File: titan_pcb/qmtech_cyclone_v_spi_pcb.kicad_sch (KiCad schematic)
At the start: 47 parts, among them J1 FPGA, J10 OLED_CONN, J11 OLED_CONN, J12 CH341_PRG_CONN, J13 SPI_HEADER, J14 SPI_HEADER, J15 I2C_PULLUP, J16 I2C_PULLUP, J17 I2C_PULLUP, J18 I2C_PULLUP, J19 Barrel_Jack_MountingPin, J2 FPGA, J20 PWR_SW, J21 PWR_SW, J22 PWR_SW, J23 PWR_SW, J3 TEENSY, J4 TEENSY, J5 ESP, J6 ESP, J7 PICO, J8 PICO, J9 OLED_JMP, U1 LM1084-3.3

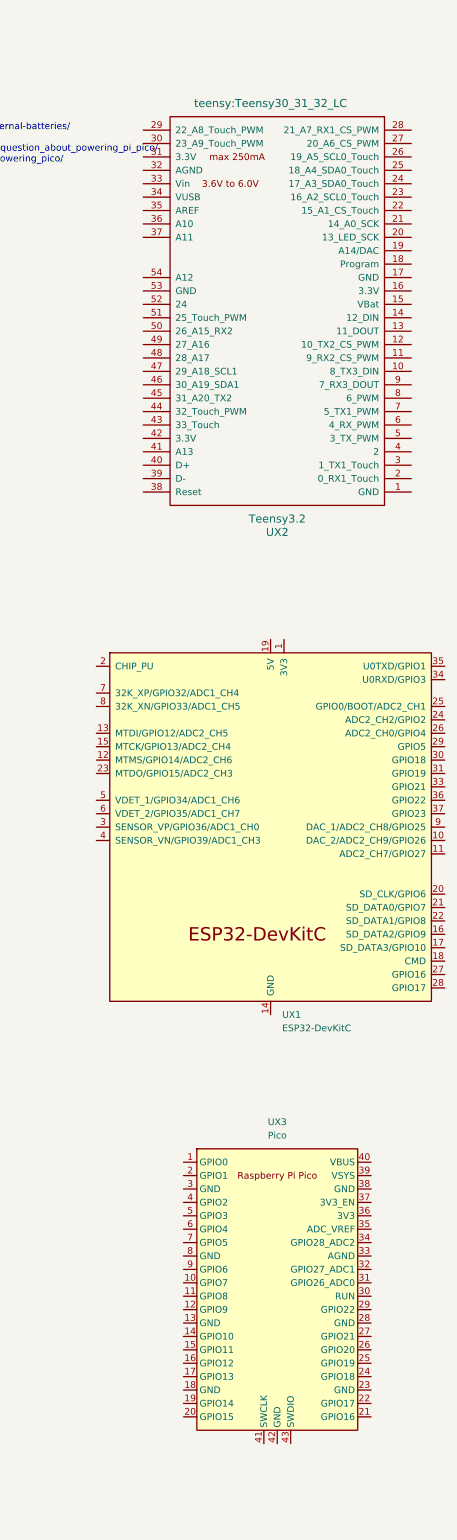
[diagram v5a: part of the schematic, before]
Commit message: removed mcus, updated silkscreen, regenerated bom
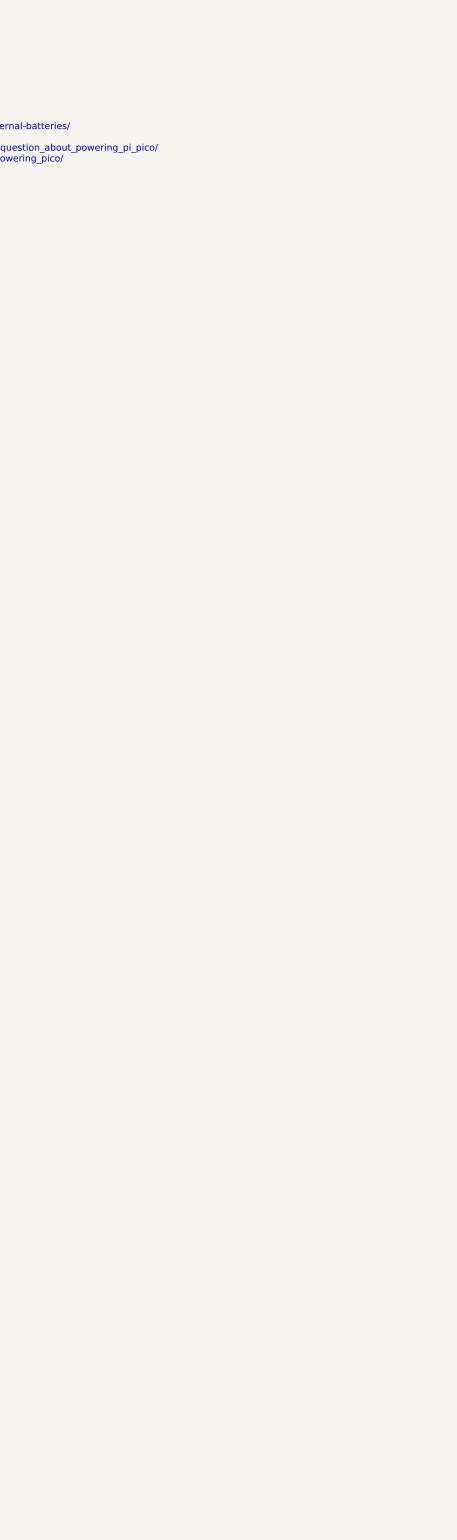
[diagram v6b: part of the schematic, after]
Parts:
- removed UX1: ESP32-DevKitC, PCM_Espressif:ESP32-DevKitC, symbol PCM_Espressif:ESP32-DevKitC
- removed UX2: Teensy3.2, teensy:Teensy30_31_32_LC, symbol teensy:Teensy3.2
- removed UX3: Pico, MCU_RaspberryPi_and_Boards:RPi_Pico_SMD_TH, symbol MCU_RaspberryPi_and_Boards:Pico
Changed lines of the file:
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@@
     )
   )
-  (symbol (lib_id "PCM_Espressif:ESP32-DevKitC") (at 491.49 163.83 0) (unit 1)
-    (in_bom no) (on_board no) (dnp no) (fields_autoplaced)
-    (property "Reference" "UX1" (at 493.6841 199.39 0)
-      (effects (font (size 1.27 1.27)) (justify left))
-    )
-    (property "Value" "ESP32-DevKitC" (at 493.6841 201.93 0)
-      (effects (font (size 1.27 1.27)) (justify left))
-    )
-    (property "Footprint" "PCM_Espressif:ESP32-DevKitC" (at 491.49 207.01 0)
-      (effects (font (size 1.27 1.27)) hide)
-    )
-    (property "Datasheet" "https://docs.espressif.com/projects/esp-idf/zh_CN/latest/esp32/hw-reference/esp32/get-started-devkitc.html" (at 491.49 209.55 0)
-      (effects (font (size 1.27 1.27)) hide)
-    )
-    (pin "14")
-    (pin "19")
+  (symbol (lib_id "Connector:AVR-JTAG-10") (at 184.785 318.135 0) (unit 1)
+    (in_bom no) (on_board yes) (dnp no) (fields_autoplaced)
+    (property "Reference" "JX1" (at 172.72 316.865 0)
+      (effects (font (size 1.27 1.27)) (justify right))
+    )
+    (property "Value" "DUMMY_JTAG" (at 172.72 319.405 0)
+      (effects (font (size 1.27 1.27)) (justify right))
+    )
+    (property "Footprint" "Connector_IDC:IDC-Header_2x05_P2.54mm_Vertical" (at 180.975 314.325 90)
+      (effects (font (size 1.27 1.27)) hide)
+    )
+    (property "Datasheet" " ~" (at 152.4 332.105 0)
+      (effects (font (size 1.27 1.27)) hide)
+    )
     (pin "1")
     (pin "10")
-    (pin "11")
-    (pin "12")
-    (pin "13")
-    (pin "15")
-    (pin "16")
-    (pin "17")
-    (pin "18")
-    (pin "2")
-    (pin "20")
-    (pin "21")
-    (pin "22")
-    (pin "23")
-    (pin "24")
-    (pin "25")
-    (pin "26")
-    (pin "27")
-    (pin "28")
-    (pin "29")
-    (pin "3")
-    (pin "30")
-    (pin "31")
-    (pin "32")
-    (pin "33")
-    (pin "34")
-    (pin "35")
-    (pin "36")
-    (pin "37")
-    (pin "38")
+    (pin "2")
+    (pin "3")
     (pin "4")
     (pin "5")
@@
       (project "qmtech_cyclone_v_spi_pcb"
         (path "/6b222715-3ff4-46c6-84bf-6d2ef29db0c3"
-          (reference "UX1") (unit 1)
-        )
-      )
-    )
-  )
-  (symbol (lib_id "Connector:AVR-JTAG-10") (at 184.785 318.135 0) (unit 1)
-    (in_bom no) (on_board yes) (dnp no) (fields_autoplaced)
-    (property "Reference" "JX1" (at 172.72 316.865 0)
-      (effects (font (size 1.27 1.27)) (justify right))
-    )
-    (property "Value" "DUMMY_JTAG" (at 172.72 319.405 0)
-      (effects (font (size 1.27 1.27)) (justify right))
-    )
-    (property "Footprint" "Connector_IDC:IDC-Header_2x05_P2.54mm_Vertical" (at 180.975 314.325 90)
-      (effects (font (size 1.27 1.27)) hide)
-    )
-    (property "Datasheet" " ~" (at 152.4 332.105 0)
-      (effects (font (size 1.27 1.27)) hide)
-    )
-    (pin "1")
-    (pin "10")
-    (pin "2")
-    (pin "3")
-    (pin "4")
-    (pin "5")
-    (pin "6")
-    (pin "7")
-    (pin "8")
-    (pin "9")
-    (instances
-      (project "qmtech_cyclone_v_spi_pcb"
-        (path "/6b222715-3ff4-46c6-84bf-6d2ef29db0c3"
           (reference "JX1") (unit 1)
         )
@@
         (path "/6b222715-3ff4-46c6-84bf-6d2ef29db0c3"
           (reference "J20") (unit 1)
-        )
-      )
-    )
-  )
-  (symbol (lib_id "MCU_RaspberryPi_and_Boards:Pico") (at 492.76 251.46 0) (unit 1)
-    (in_bom no) (on_board no) (dnp no) (fields_autoplaced)
-    (property "Reference" "UX3" (at 492.76 219.71 0)
-      (effects (font (size 1.27 1.27)))
-    )
-    (property "Value" "Pico" (at 492.76 222.25 0)
-      (effects (font (size 1.27 1.27)))
-    )
-    (property "Footprint" "MCU_RaspberryPi_and_Boards:RPi_Pico_SMD_TH" (at 492.76 251.46 90)
-      (effects (font (size 1.27 1.27)) hide)
-    )
-    (property "Datasheet" "" (at 492.76 251.46 0)
-      (effects (font (size 1.27 1.27)) hide)
-    )
-    (pin "1")
-    (pin "10")
-    (pin "11")
-    (pin "12")
-    (pin "13")
-    (pin "14")
-    (pin "15")
-    (pin "16")
-    (pin "17")
-    (pin "18")
-    (pin "19")
-    (pin "2")
-    (pin "20")
-    (pin "21")
-    (pin "22")
-    (pin "23")
-    (pin "24")
-    (pin "25")
-    (pin "26")
-    (pin "27")
-    (pin "28")
-    (pin "29")
-    (pin "3")
-    (pin "30")
-    (pin "31")
-    (pin "32")
-    (pin "33")
-    (pin "34")
-    (pin "35")
-    (pin "36")
-    (pin "37")
-    (pin "38")
-    (pin "39")
-    (pin "4")
-    (pin "40")
-    (pin "41")
-    (pin "42")
-    (pin "43")
-    (pin "5")
-    (pin "6")
-    (pin "7")
-    (pin "8")
-    (pin "9")
-    (instances
-      (project "qmtech_cyclone_v_spi_pcb"
-        (path "/6b222715-3ff4-46c6-84bf-6d2ef29db0c3"
-          (reference "UX3") (unit 1)
         )
       )
@@
         )
       )
-    )
-  )
-  (symbol (lib_id "teensy:Teensy3.2") (at 492.76 66.04 180) (unit 1)
-    (in_bom no) (on_board no) (dnp no)
-    (property "Reference" "UX2" (at 492.76 107.95 0)
-      (effects (font (size 1.524 1.524)))
-    )
-    (property "Value" "Teensy3.2" (at 492.76 105.41 0)
-      (effects (font (size 1.524 1.524)))
-    )
-    (property "Footprint" "teensy:Teensy30_31_32_LC" (at 491.49 26.67 0)
-      (effects (font (size 1.524 1.524)))
-    )
-    (property "Datasheet" "" (at 492.76 46.99 0)
-      (effects (font (size 1.524 1.524)))
-    )
-    (pin "1")
-    (pin "10")
-    (pin "11")
-    (pin "12")
-    (pin "13")
-    (pin "14")
-    (pin "15")
-    (pin "16")
-    (pin "17")
-    (pin "18")
-    (pin "19")
-    (pin "2")
-    (pin "20")
-    (pin "21")
-    (pin "22")
-    (pin "23")
-    (pin "24")
-    (pin "25")
-    (pin "26")
-    (pin "27")
-    (pin "28")
-    (pin "29")
-    (pin "3")
-    (pin "30")
-    (pin "31")
-    (pin "32")
-    (pin "33")
-    (pin "34")
-    (pin "35")
-    (pin "36")
-    (pin "37")
-    (pin "38")
-    (pin "39")
-    (pin "4")
-    (pin "40")
-    (pin "41")
-    (pin "42")
-    (pin "43")
-    (pin "44")
-    (pin "45")
-    (pin "46")
-    (pin "47")
-    (pin "48")
-    (pin "49")
-    (pin "5")
-    (pin "50")
-    (pin "51")
-    (pin "52")
-    (pin "53")
-    (pin "54")
-    (pin "6")
-    (pin "7")
-    (pin "8")
-    (pin "9")
-    (instances
-      (project "qmtech_cyclone_v_spi_pcb"
-        (path "/6b222715-3ff4-46c6-84bf-6d2ef29db0c3"
-          (reference "UX2") (unit 1)
-        )
-      )

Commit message: updated pcb
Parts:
- added SW1: PICO_RESET_SW, Button_Switch_THT:SW_PUSH_6mm_H5mm, symbol Switch:SW_Push
- renumbered R8 to R1, R7 to R2, R6 to R3, R5 to R4, R4 to R5, R3 to R6, R2 to R7, R1 to R8
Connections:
- net GND: now also SW1.2
- net PICO_RUN: now also SW1.1
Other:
- moved on the sheet: H1, H2, H3, H4, H5, H6, H7, H8, JX1
